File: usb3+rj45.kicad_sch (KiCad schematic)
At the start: 67 parts, among them J1 RJE361882415, T1 Choke_SRF2012A-801Y, T2 Choke_SRF2012A-801Y, T3 Choke_SRF2012A-801Y, T4 Choke_SRF2012A-801Y, T5 Trans_SM453229-381N7Y, T6 Trans_SM453229-381N7Y, T7 Trans_SM453229-381N7Y, T8 Trans_SM453229-381N7Y, U1 ESD204DQAR, U2 ESD204DQAR, U3 AP22615A_TSOT26, U4 AP22615A_TSOT26

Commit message: Optimize BOM, reannotate
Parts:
- removed C19, C20: C_10u_0603, antmicro-footprints:C_0603_1608Metric, symbol antmicroCapacitors0603:C_10u_0603
- removed C4, C5: C_Pol_100u_10V_KYOCERA-AVX-TLJ-A, antmicro-footprints:C_Pol_EIA-A, symbol antmicroCapacitorspol:C_Pol_100u_10V_KYOCERA-AVX-TLJ-A
- added C19, C20: C_22u_16V_0603, antmicro-footprints:C_0603_1608Metric, symbol antmicroCapacitors0603:C_22u_16V_0603
- added C3, C4: C_Pol_100u_10V_KEMET-T520-B, antmicro-footprints:C_Pol_EIA-B, symbol antmicroCapacitorspol:C_Pol_100u_10V_KEMET-T520-B
- renumbered C3 to C5
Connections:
- net +5V: now also C19.2, C20.2
- net GND: now also C19.1, C20.1, C3.2, C4.2
- net P1_VBUS: now also C3.1
- net P2_VBUS: now also C4.1

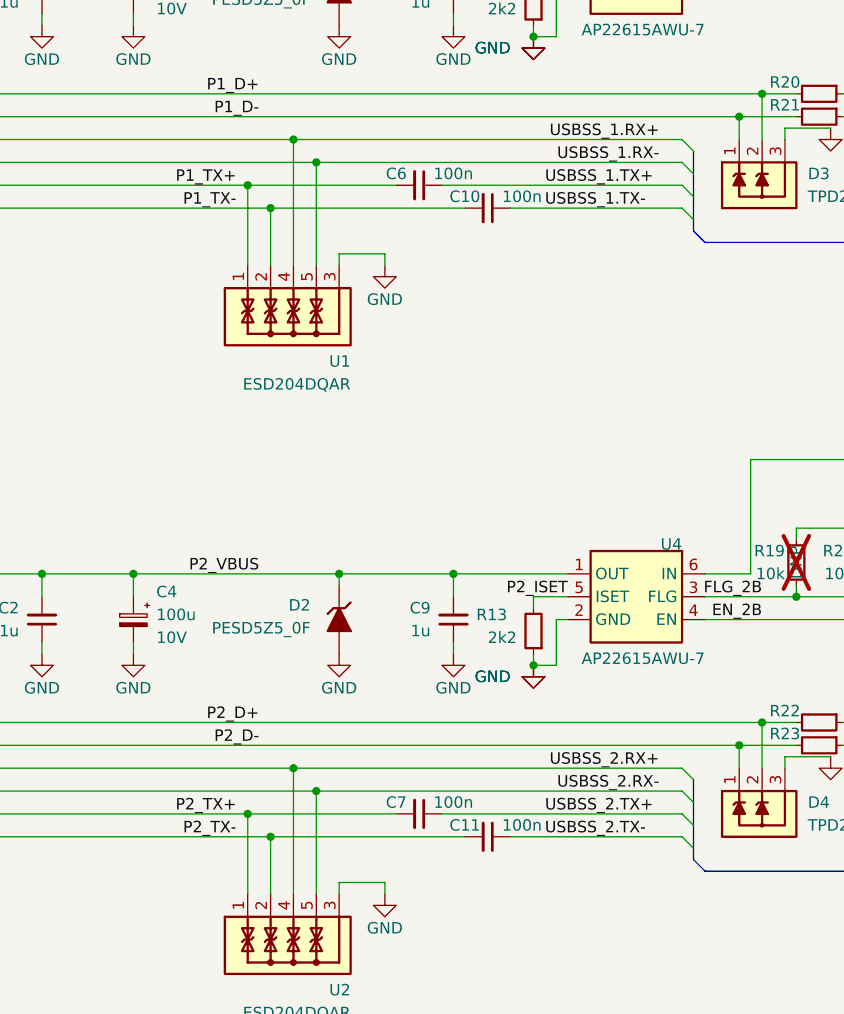
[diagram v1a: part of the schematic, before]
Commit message: [#58904] Remove caps from USBSS connectors
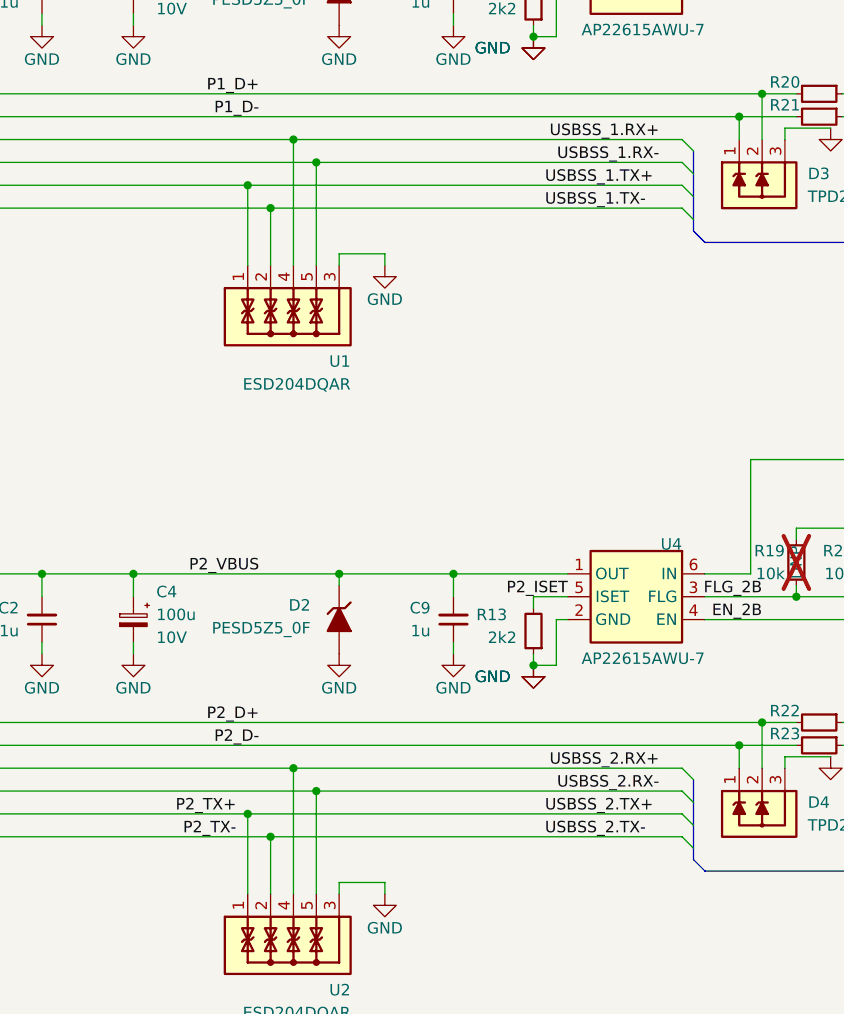
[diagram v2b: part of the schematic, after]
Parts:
- removed C10, C11, C6, C7: C_100n_0402, antmicro-footprints:C_0402_1005Metric, symbol antmicroCapacitors0402:C_100n_0402
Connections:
- net P1_TX+ is gone; now on net USBSS_1.TX+: J1.U9 (SSTX+), U1.1, U1.10
- net P1_TX- is gone; now on net USBSS_1.TX-: J1.U8 (SSTX-), U1.2, U1.9

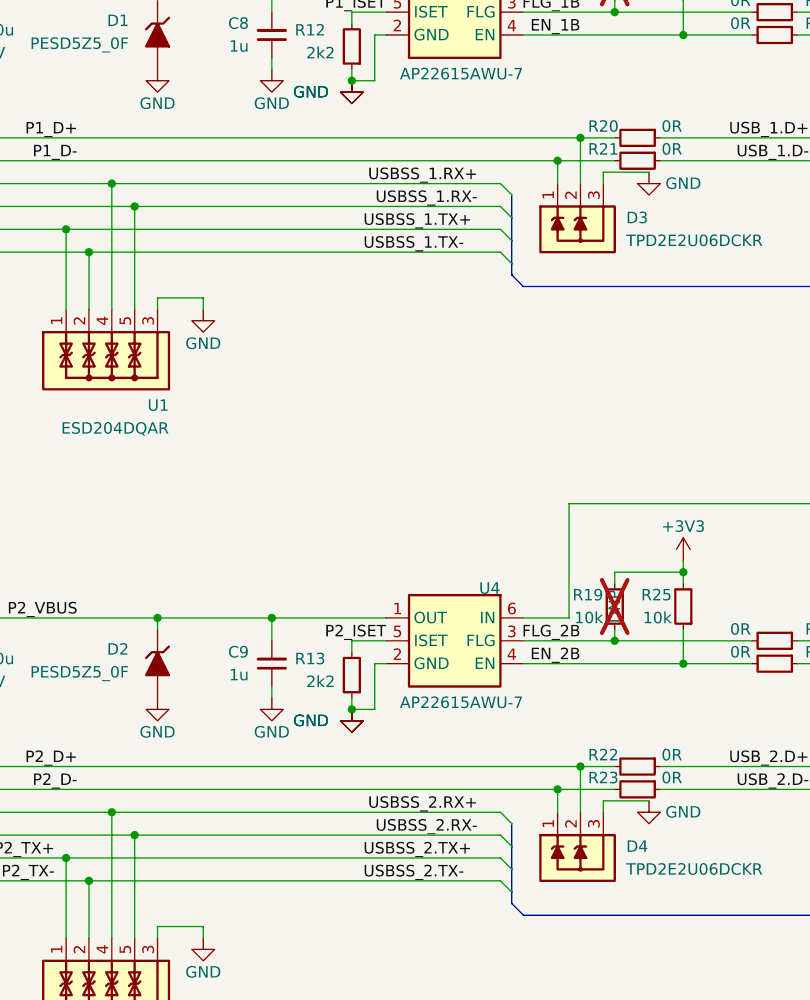
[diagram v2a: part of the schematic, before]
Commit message: [#58904] Change pinout of backplane connector. Connect CLKREQ from PCIe devices
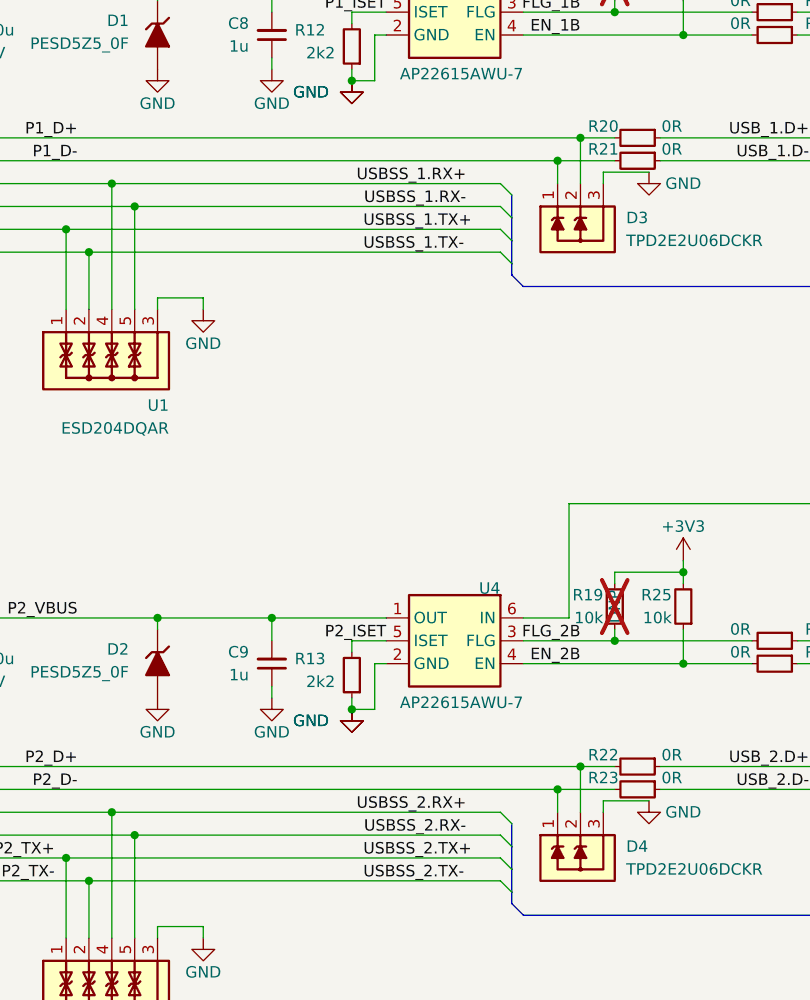
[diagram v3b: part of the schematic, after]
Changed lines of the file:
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@@
     (effects (font (size 1.27 1.27)) (justify left bottom))
   )
-  (label "USBSS_2.RX-" (at 218.44 248.92 180) (fields_autoplaced)
+  (label "USBSS_2.RX-" (at 217.17 248.92 180) (fields_autoplaced)
     (effects (font (size 1.27 1.27)) (justify right bottom))
   )
@@
     (effects (font (size 1.27 1.27)) (justify right bottom))
   )
-  (label "USBSS_1.RX-" (at 218.44 179.07 180) (fields_autoplaced)
+  (label "USBSS_1.RX-" (at 217.17 179.07 180) (fields_autoplaced)
     (effects (font (size 1.27 1.27)) (justify right bottom))
   )
@@
     (effects (font (size 1.27 1.27)) (justify right bottom))
   )
-  (label "USBSS_2.RX+" (at 218.44 246.38 180) (fields_autoplaced)
+  (label "USBSS_2.RX+" (at 217.17 246.38 180) (fields_autoplaced)
     (effects (font (size 1.27 1.27)) (justify right bottom))
   )
@@
     (effects (font (size 1.27 1.27)) (justify right bottom))
   )
-  (label "USBSS_1.RX+" (at 218.44 176.53 180) (fields_autoplaced)
+  (label "USBSS_1.RX+" (at 217.17 176.53 180) (fields_autoplaced)
     (effects (font (size 1.27 1.27)) (justify right bottom))
   )

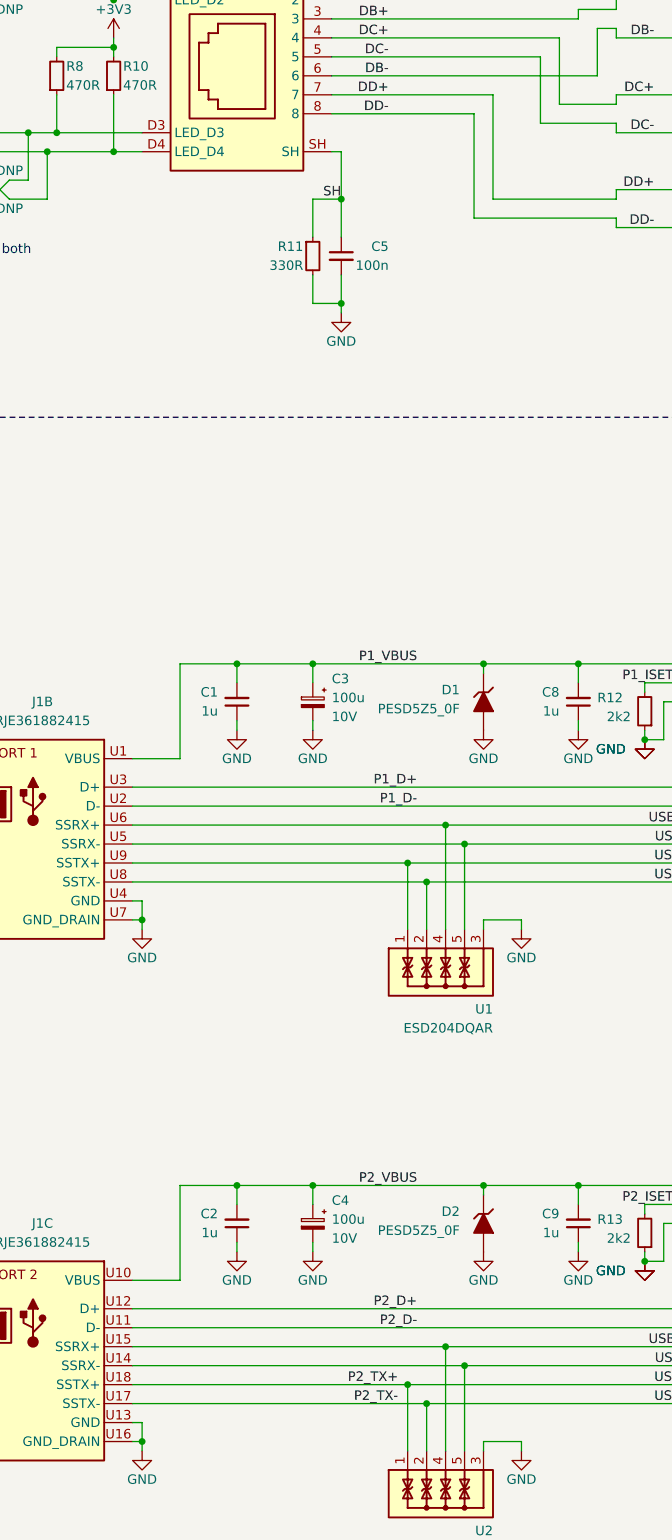
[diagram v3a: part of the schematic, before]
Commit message: [#58904] Fix DRC
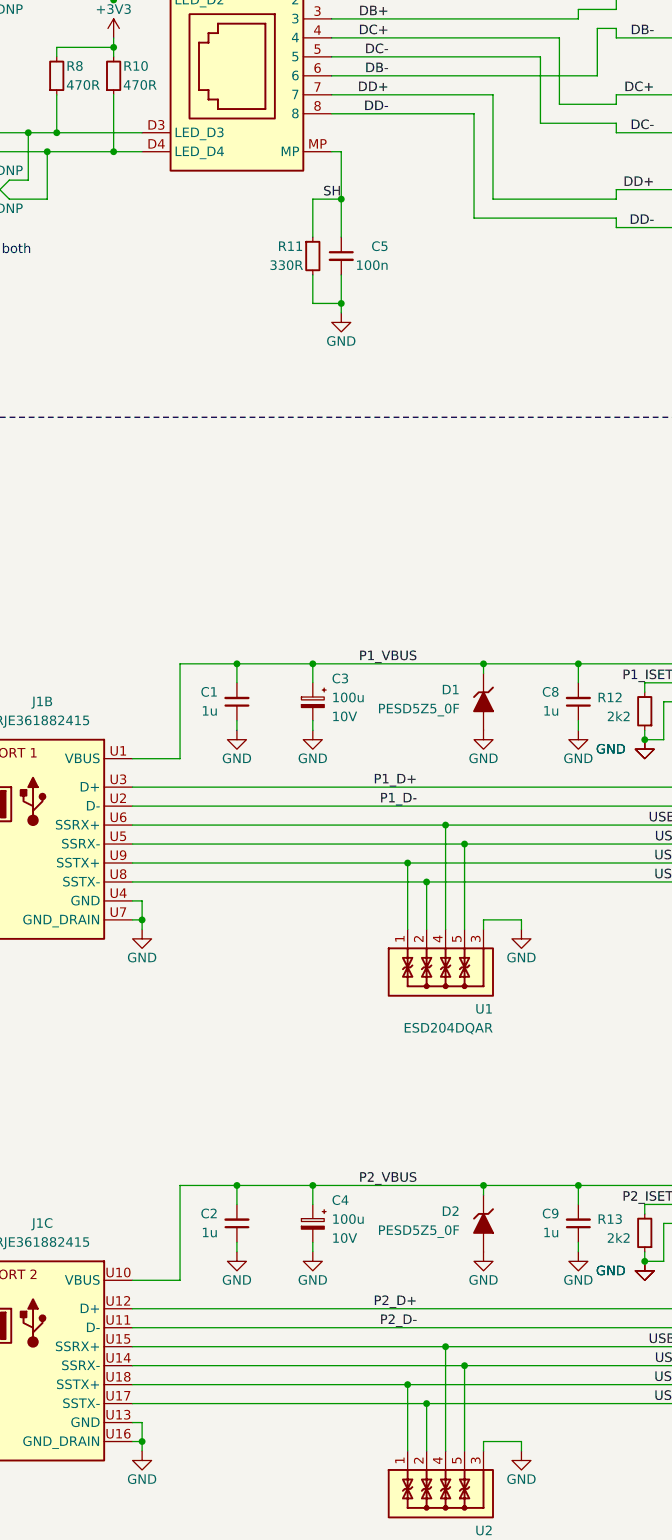
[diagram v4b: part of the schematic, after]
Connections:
- net SH: now also J1.MP; no longer J1.SH
- net P2_TX+ renamed USBSS_2.TX+
- net P2_TX- renamed USBSS_2.TX-
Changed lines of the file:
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@@
     (effects (font (size 1.27 1.27)) (justify left bottom))
   )
-  (label "P2_TX-" (at 171.45 254 180) (fields_autoplaced)
-    (effects (font (size 1.27 1.27)) (justify right bottom))
-  )
   (label "FLG_1B" (at 229.87 157.48 180) (fields_autoplaced)
-    (effects (font (size 1.27 1.27)) (justify right bottom))
-  )
-  (label "P2_TX+" (at 171.45 251.46 180) (fields_autoplaced)
     (effects (font (size 1.27 1.27)) (justify right bottom))
   )
@@
     )
   )
-  (symbol (lib_id "antmicroModularConnectorsJacks:Amphenol_RJE361882415") (at 162.56 63.5 0) (mirror y) (unit 1)
+  (symbol (lib_name "Amphenol_RJE361882415_1") (lib_id "antmicroModularConnectorsJacks:Amphenol_RJE361882415") (at 162.56 63.5 0) (mirror y) (unit 1)
     (in_bom yes) (on_board yes) (dnp no) (fields_autoplaced)
     (property "Reference" "J1" (at 149.86 55.88 0)
@@
     (pin "U1")
     (pin "8")
-    (pin "SH")
+    (pin "MP")
     (pin "U15")
     (pin "6")

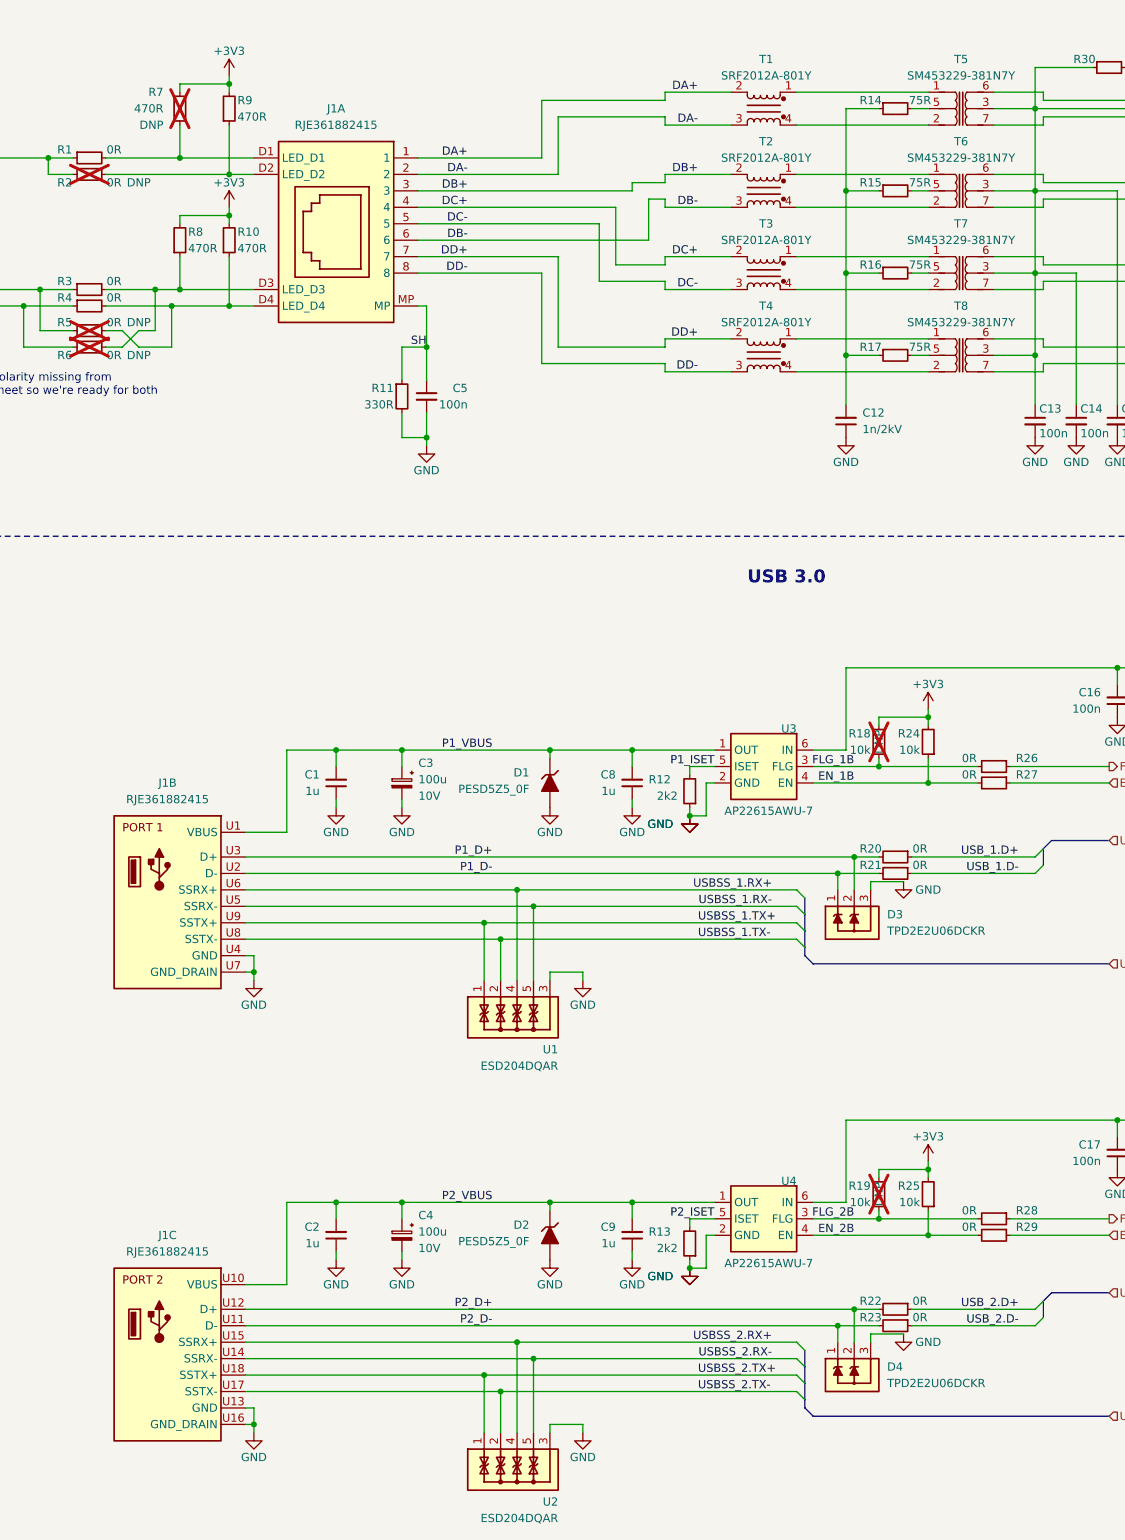
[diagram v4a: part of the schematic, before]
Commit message: Update components from the library
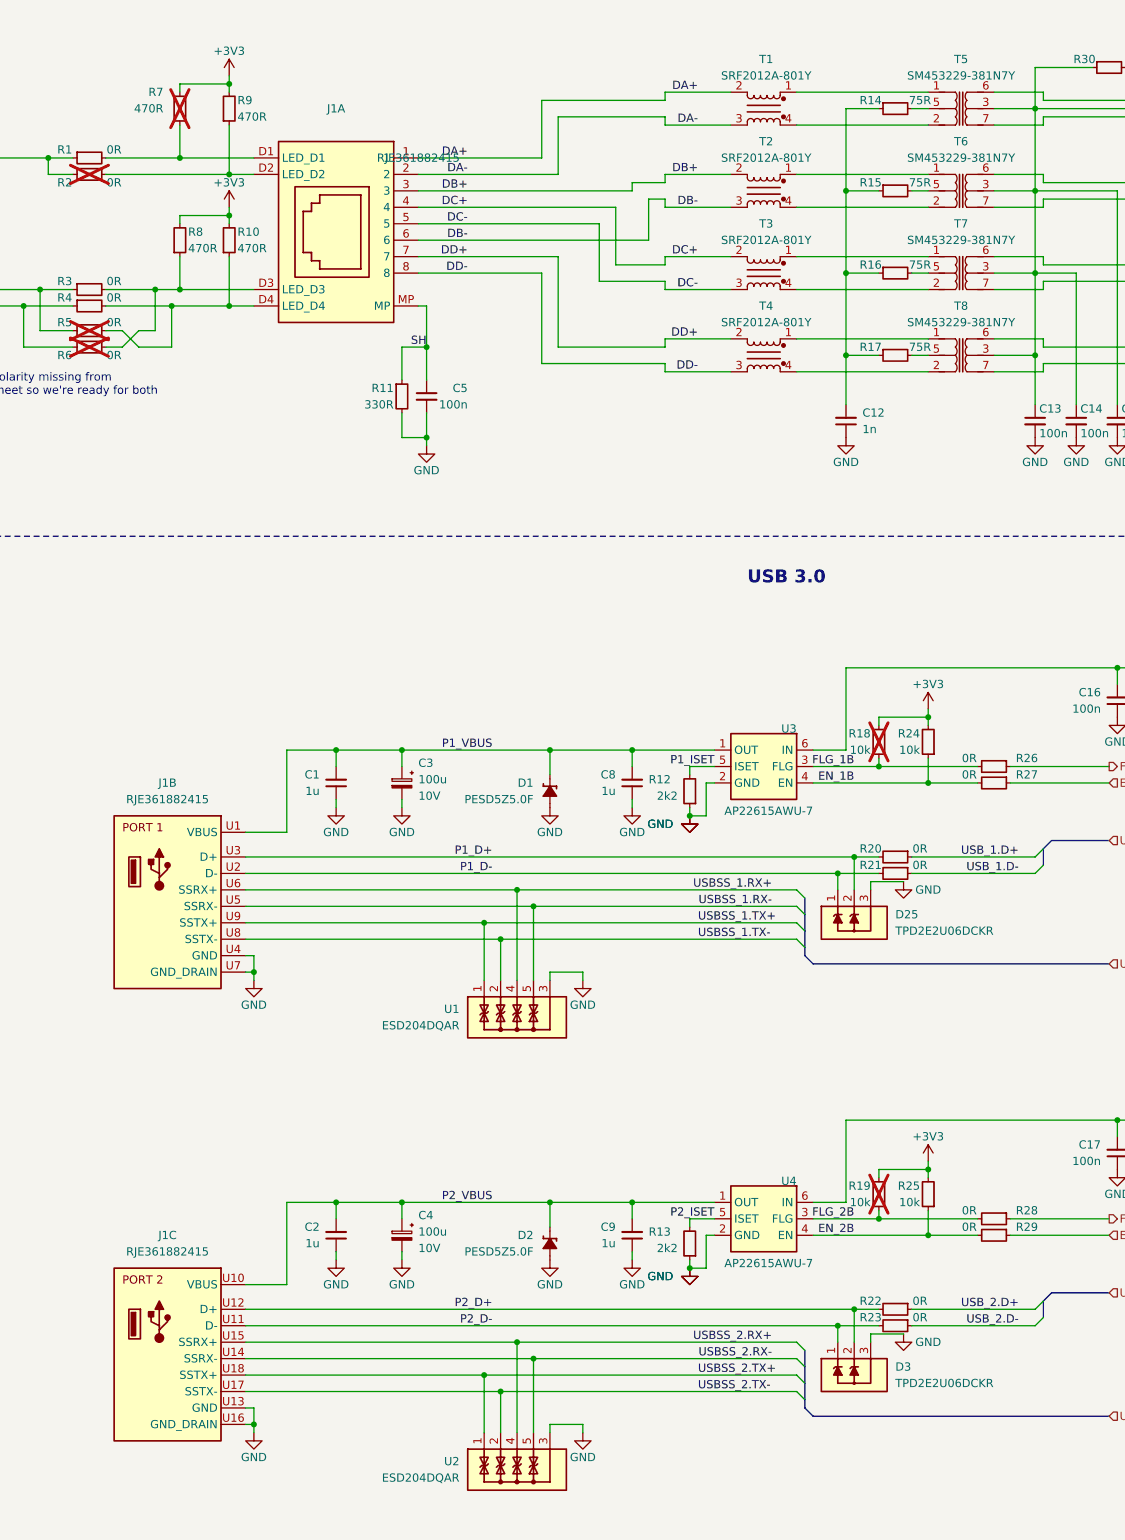
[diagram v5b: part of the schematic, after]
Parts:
- removed D3, D4: TPD2E2U06DCKR, antmicro-footprints:SC70-3, symbol antmicroTVSDiodes:TPD2E2U06DCKR
- added D25, D3: TPD2E2U06_SC70, antmicro-footprints:SC70-3, symbol antmicroTVSDiodes:TPD2E2U06_SC70
- C1, C13, C14, C15, C16, C17, C18, C19, C2, C20, C3, C4, C5, C8, C9, D1, D2, R1, R10, R11, R12, R13, R14, R15, R16, R17, R20, R21, R22, R23, R26, R27, R28, R29, R3, R30, R4, R8, R9, T1, T2, T3, T4: Public (none) -> False
- C12: Public (none) -> False; Val 1n/2kV -> 1n; Voltage (none) -> 2kV
- J1: value RJE361882415 -> Amphenol_RJE361882415
- R18, R19, R24, R25: DNP DNP -> (none); Public (none) -> False; now in the parts list
- R2, R5, R6, R7: DNP DNP -> (none); Public (none) -> False
- U3, U4: MPN AP22615AWU-7 -> AP22615AWU-7
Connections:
- net GND: now also D25.3, D3.3
- net P1_D+: now also D25.2
- net P1_D-: now also D25.1
- net P2_D+: now also D3.2
- net P2_D-: now also D3.1
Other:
- moved on the sheet: U1, U2
